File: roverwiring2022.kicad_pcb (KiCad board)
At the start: 2 copper layers, 78.7 x 116.8 mm, 20 parts, among them J1 Conn_01x19, J10 Conn_01x05, J11 Conn_01x05, J12 Conn_01x05, J13 Conn_01x05, J2 Conn_01x19, J3 Conn_01x09, J4 Conn_01x04, J5 Conn_01x04, J6 Conn_01x04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

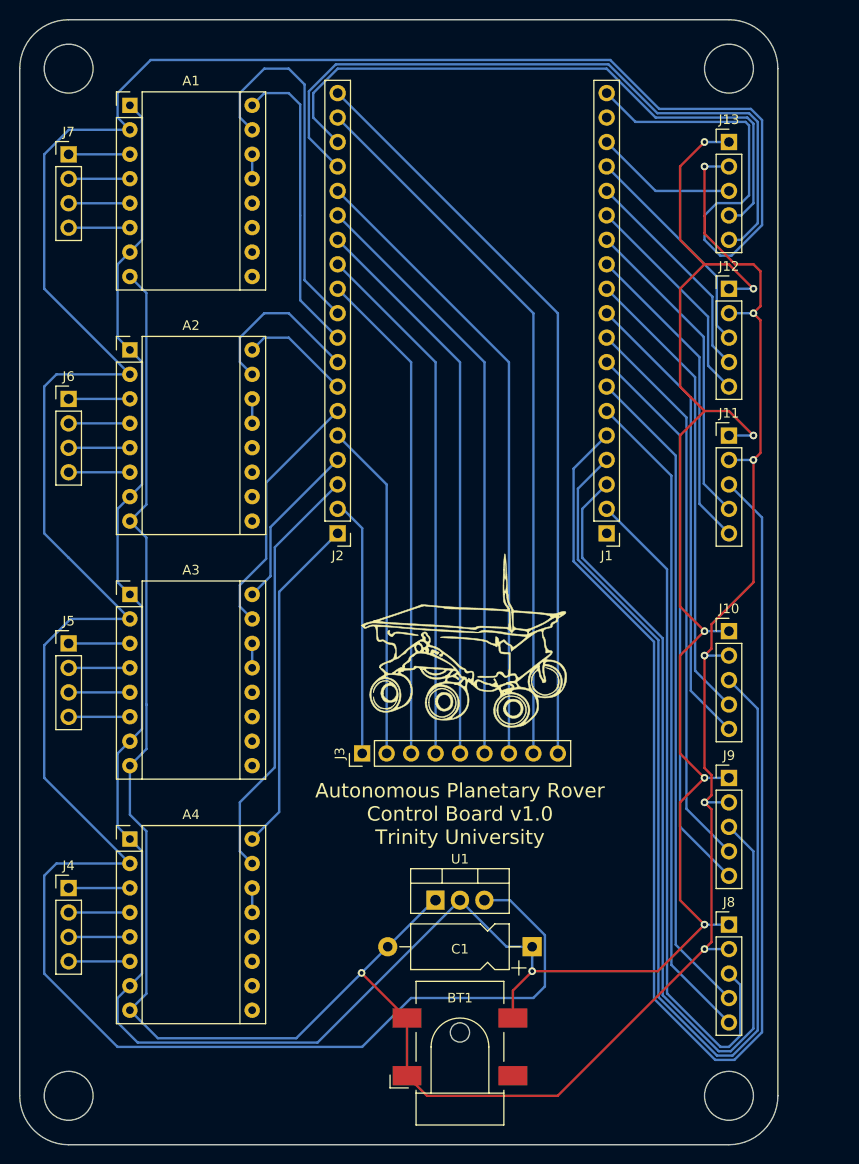
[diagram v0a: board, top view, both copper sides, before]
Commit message: updating traces to clear drc errors, widening power traces
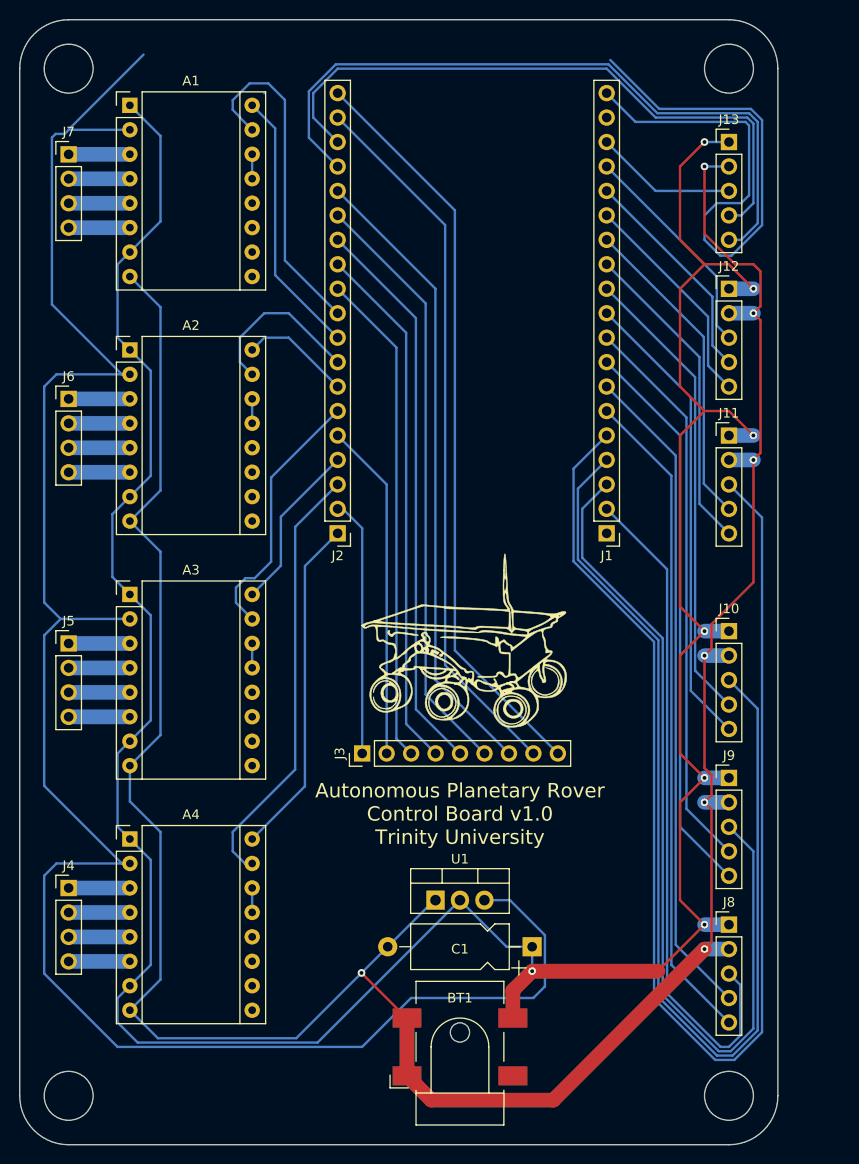
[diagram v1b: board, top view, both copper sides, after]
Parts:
- BT1: value 24V -> 12V
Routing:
- net /VDD: track 326.2 -> 278.8 mm
- net GND: track 302.6 -> 306.9 mm
- net Net-(A1-Pad16): track 31.8 -> 27.8 mm
- net /VCC: track 274.3 -> 278.3 mm
- net Net-(A1-Pad15): track 38.0 -> 35.2 mm
- net Net-(A4-Pad15): track 44.1 -> 45.2 mm
- net Net-(A3-Pad15): track 26.3 -> 27.2 mm

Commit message: resolved all outstanding drc conflicts and finished VCC and GND planes
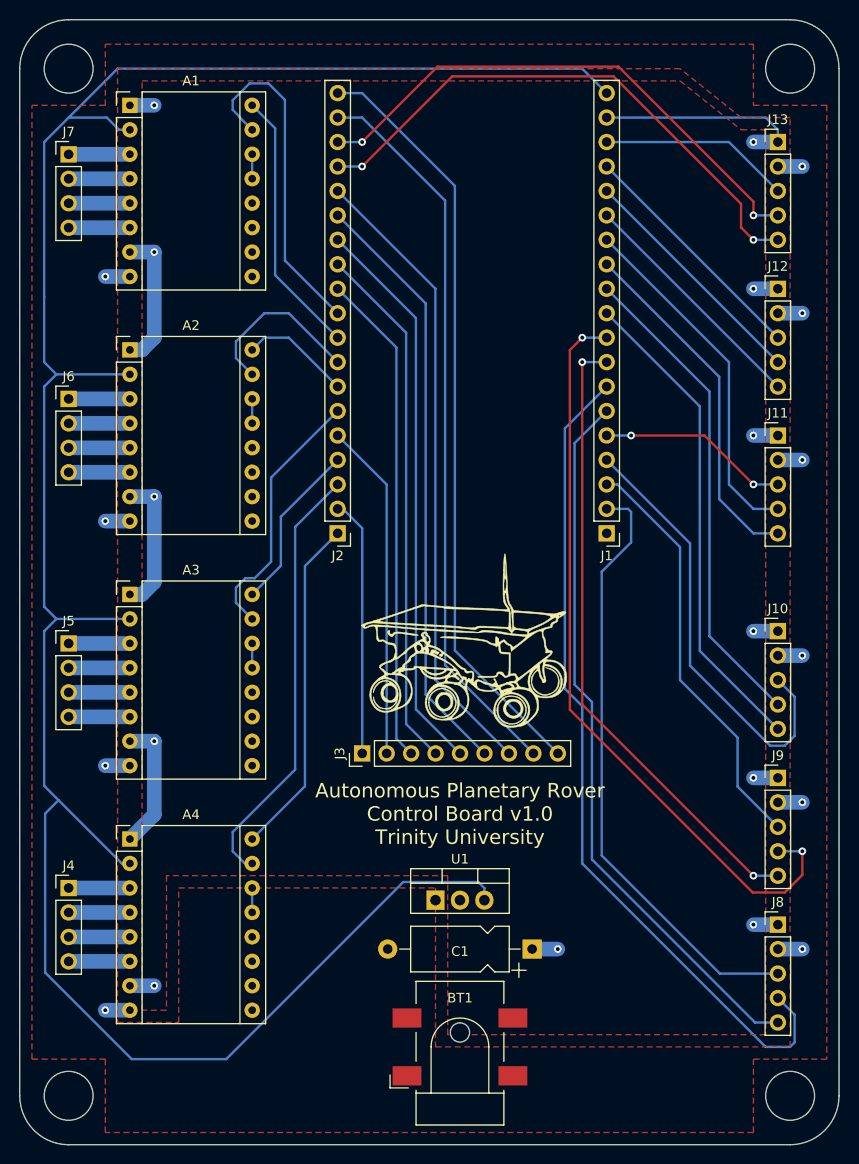
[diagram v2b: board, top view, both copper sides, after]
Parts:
- moved J10 5.08 mm to (261.6, 104.1)
- moved J11 5.08 mm to (261.6, 83.8)
- moved J12 5.08 mm to (261.6, 68.6)
- moved J13 5.08 mm to (261.6, 53.3)
- moved J8 5.08 mm to (261.6, 134.6)
- moved J9 5.08 mm to (261.6, 119.4)
- moved C1 0.24 mm to (236.1, 137.2)
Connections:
- J1 pad 18: unconnected-(J1-Pad18) -> GND
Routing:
- net /VCC: track 278.3 -> 25.4 mm, vias 7 -> 10
- net GND: track 306.9 -> 85.3 mm, vias 7 -> 12
- net Net-(J1-Pad5): track 136.7 -> 19.9 mm, vias 0 -> 2
- net Net-(J1-Pad4): track 112.0 -> 46.2 mm
- net Net-(J1-Pad3): track 92.4 -> 43.6 mm
- net /VDD: track 278.8 -> 242.9 mm
- net Net-(J1-Pad9): track 58.6 -> 79.5 mm, vias 0 -> 2
- net Net-(J1-Pad7): track 68.8 -> 87.5 mm
- net Net-(J13-Pad5): track 73.5 -> 58.1 mm, vias 0 -> 2
- net Net-(J13-Pad4): track 66.6 -> 56.2 mm, vias 0 -> 2
- net Net-(J1-Pad2): track 70.2 -> 63.0 mm
- net Net-(J1-Pad8): track 58.6 -> 65.8 mm, vias 0 -> 2
- net Net-(J1-Pad6): track 68.8 -> 75.0 mm
- net Net-(J1-Pad17): track 14.8 -> 19.9 mm
- net Net-(J1-Pad13): track 33.2 -> 36.8 mm
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- added copper zone on F.Cu, net /VCC
- added copper zone on F.Cu, net GND
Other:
- board size 78.7 x 116.8 mm -> 85.1 x 116.8 mm

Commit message: reshaped power planes, fixed gnd issue
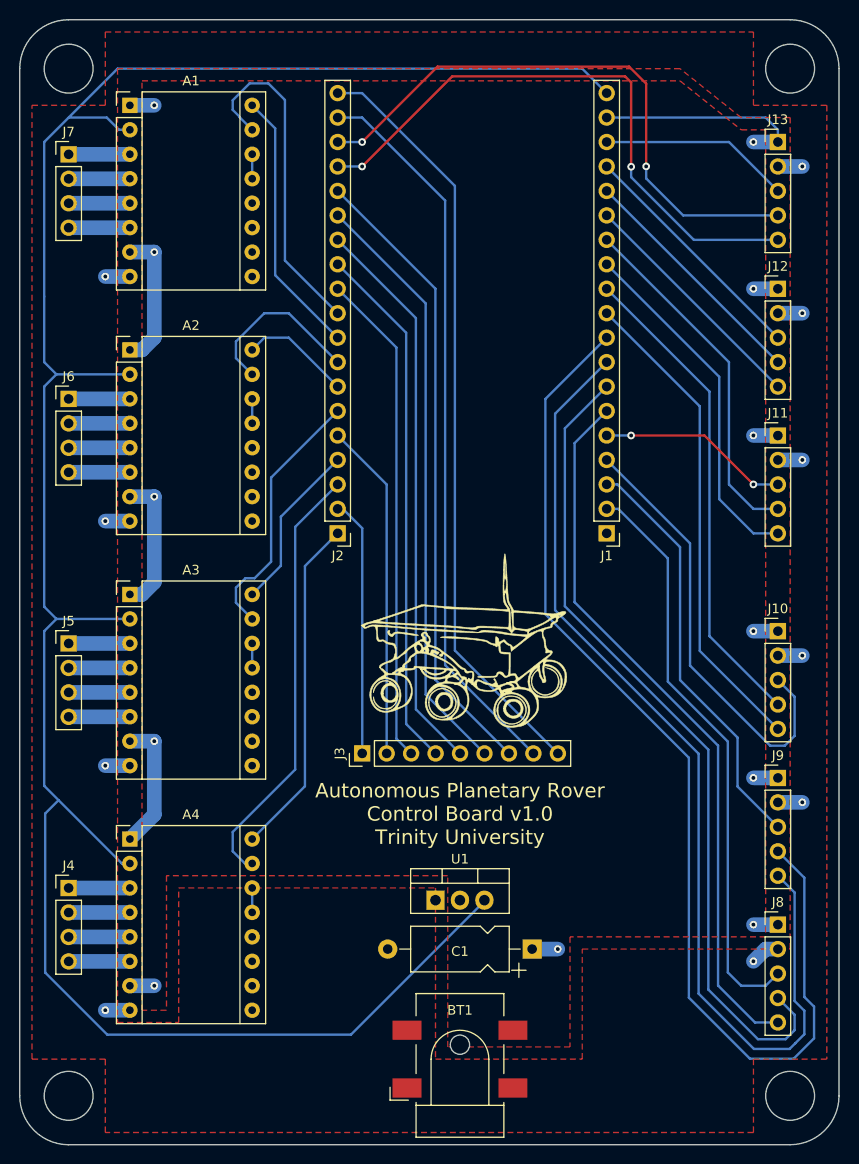
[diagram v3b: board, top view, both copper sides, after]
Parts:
- moved BT1 1.27 mm to (228.6, 148.6)
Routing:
- net Net-(J1-Pad8): track 65.8 -> 105.6 mm, vias 2 -> 0
- net Net-(J1-Pad9): track 79.5 -> 114.8 mm, vias 2 -> 0
- net Net-(J13-Pad4): track 56.2 -> 61.1 mm
- net /VDD: track 242.9 -> 238.6 mm
- net Net-(J13-Pad5): track 58.1 -> 62.4 mm
- net Net-(J1-Pad2): track 63.0 -> 60.4 mm
- net Net-(J1-Pad7): track 87.5 -> 86.1 mm
- net /VCC: track 25.4 -> 26.0 mm

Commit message: added backside ground plane
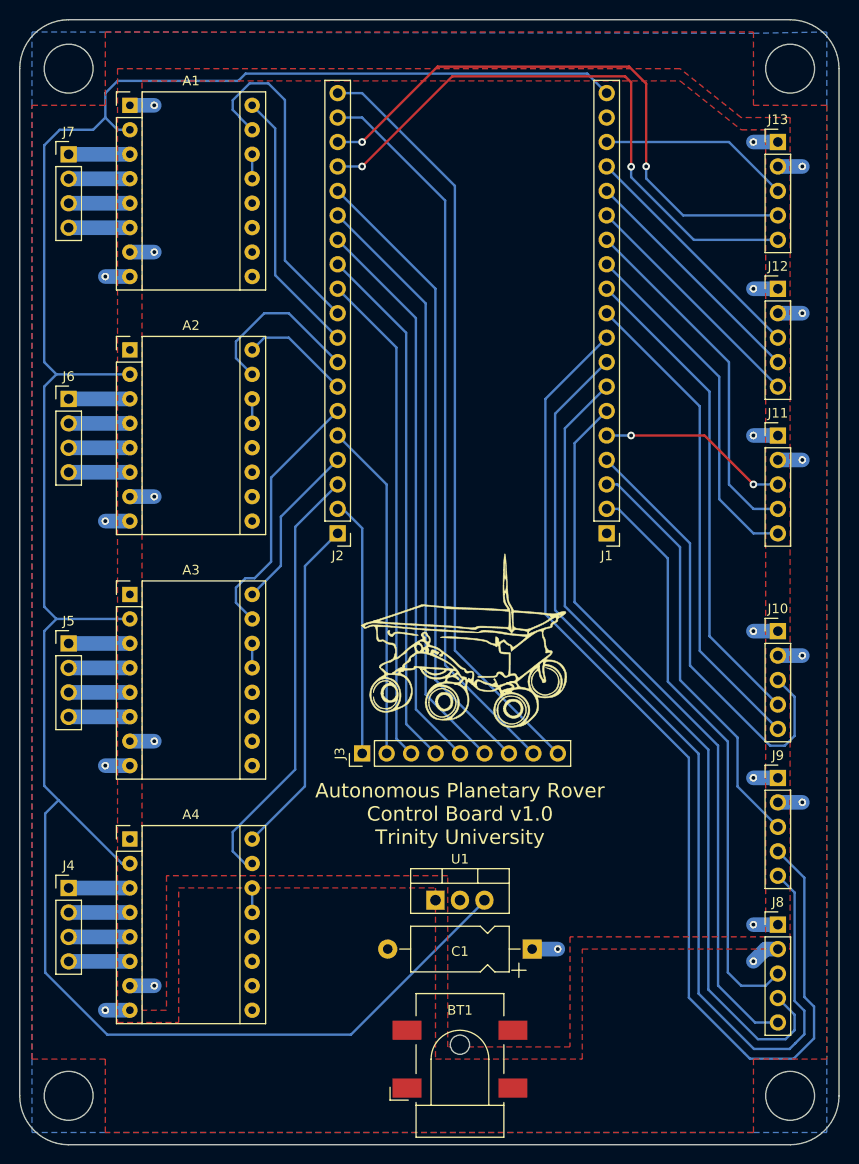
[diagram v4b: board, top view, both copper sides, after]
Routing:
- net GND: track 85.3 -> 30.7 mm
- net /VDD: track 238.6 -> 235.6 mm
- added copper zone on B.Cu, net GND
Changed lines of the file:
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@@
   )
   (segment (start 194.32 102.87) (end 186.69 102.87) (width 0.25) (layer "B.Cu") (net 1))
-  (segment (start 193.18863 52.07) (end 191.91863 50.8) (width 0.25) (layer "B.Cu") (net 1))
   (segment (start 185.521819 123.088181) (end 186.913 121.697) (width 0.25) (layer "B.Cu") (net 1))
+  (segment (start 241.81648 46.23648) (end 243.84 48.26) (width 0.25) (layer "B.Cu") (net 1))
   (segment (start 217.278267 146.05) (end 191.973638 146.05) (width 0.25) (layer "B.Cu") (net 1))
   (segment (start 194.32 77.47) (end 186.69 77.47) (width 0.25) (layer "B.Cu") (net 1))
+  (segment (start 187.036978 52.07) (end 190.5 52.07) (width 0.25) (layer "B.Cu") (net 1))
   (segment (start 186.69 102.87) (end 185.42 104.14) (width 0.25) (layer "B.Cu") (net 1))
   (segment (start 191.973638 146.05) (end 185.521819 139.598181) (width 0.25) (layer "B.Cu") (net 1))
+  (segment (start 185.42 53.686978) (end 187.036978 52.07) (width 0.25) (layer "B.Cu") (net 1))
+  (segment (start 191.77 48.26) (end 193.04 46.99) (width 0.25) (layer "B.Cu") (net 1))
   (segment (start 185.42 101.6) (end 186.69 102.87) (width 0.25) (layer "B.Cu") (net 1))
   (segment (start 185.42 120.204) (end 186.913 121.697) (width 0.25) (layer "B.Cu") (net 1))
   (segment (start 185.521819 139.598181) (end 185.521819 123.088181) (width 0.25) (layer "B.Cu") (net 1))
   (segment (start 185.42 78.74) (end 185.42 101.6) (width 0.25) (layer "B.Cu") (net 1))
+  (segment (start 205.579494 46.99) (end 206.333015 46.23648) (width 0.25) (layer "B.Cu") (net 1))
   (segment (start 186.69 77.47) (end 185.42 78.74) (width 0.25) (layer "B.Cu") (net 1))
   (segment (start 231.14 132.08) (end 231.14 132.188267) (width 0.25) (layer "B.Cu") (net 1))
+  (segment (start 194.32 52.07) (end 193.04 52.07) (width 0.25) (layer "B.Cu") (net 1))
+  (segment (start 186.69 77.47) (end 185.42 76.2) (width 0.25) (layer "B.Cu") (net 1))
   (segment (start 193.486 128.27) (end 194.32 128.27) (width 0.25) (layer "B.Cu") (net 1))
+  (segment (start 185.42 76.2) (end 185.42 53.686978) (width 0.25) (layer "B.Cu") (net 1))
   (segment (start 231.14 132.188267) (end 217.278267 146.05) (width 0.25) (layer "B.Cu") (net 1))
   (segment (start 186.913 121.697) (end 193.486 128.27) (width 0.25) (layer "B.Cu") (net 1))
-  (segment (start 191.91863 50.8) (end 187.96 50.8) (width 0.25) (layer "B.Cu") (net 1))
+  (segment (start 193.04 46.99) (end 205.579494 46.99) (width 0.25) (layer "B.Cu") (net 1))
   (segment (start 185.42 104.14) (end 185.42 120.204) (width 0.25) (layer "B.Cu") (net 1))
-  (segment (start 241.3 45.72) (end 243.84 48.26) (width 0.25) (layer "B.Cu") (net 1))
-  (segment (start 194.32 52.07) (end 193.18863 52.07) (width 0.25) (layer "B.Cu") (net 1))
-  (segment (start 185.42 69.404) (end 185.42 53.34) (width 0.25) (layer "B.Cu") (net 1))
-  (segment (start 185.42 69.404) (end 185.42 76.2) (width 0.25) (layer "B.Cu") (net 1))
-  (segment (start 185.42 76.2) (end 186.69 77.47) (width 0.25) (layer "B.Cu") (net 1))
-  (segment (start 193.04 45.72) (end 241.3 45.72) (width 0.25) (layer "B.Cu") (net 1))
-  (segment (start 185.42 53.34) (end 193.04 45.72) (width 0.25) (layer "B.Cu") (net 1))
+  (segment (start 190.5 52.07) (end 191.77 50.8) (width 0.25) (layer "B.Cu") (net 1))
+  (segment (start 193.04 52.07) (end 191.77 50.8) (width 0.25) (layer "B.Cu") (net 1))
+  (segment (start 206.333015 46.23648) (end 241.81648 46.23648) (width 0.25) (layer "B.Cu") (net 1))
+  (segment (start 191.77 50.8) (end 191.77 48.26) (width 0.25) (layer "B.Cu") (net 1))
   (segment (start 194.31 54.62) (end 194.32 54.61) (width 0.25) (layer "B.Cu") (net 2))
   (segment (start 187.96 54.62) (end 194.31 54.62) (width 1.524) (layer "B.Cu") (net 2))
@@
   (segment (start 263.356511 131.281511) (end 261.62 129.545) (width 0.25) (layer "B.Cu") (net 54))
   (segment (start 264.368031 146.002475) (end 264.368031 143.562525) (width 0.25) (layer "B.Cu") (net 54))
-  (segment (start 263.25646 148.544551) (end 258.71354 148.544551) (width 0.25) (layer "B.Cu") (net 55))
-  (segment (start 252.37388 142.204891) (end 252.37388 117.28641) (width 0.25) (layer "B.Cu") (net 55))
-  (segment (start 261.62 127.005) (end 264.368031 129.753031) (width 0.25) (layer "B.Cu") (net 55))
-  (segment (start 265.37955 146.421461) (end 263.25646 148.544551) (width 0.25) (layer "B.Cu") (net 55))
-  (segment (start 258.71354 148.544551) (end 252.37388 142.204891) (width 0.25) (layer "B.Cu") (net 55))
   (segment (start 237.471951 102.38448) (end 237.471951 80.028049) (width 0.25) (layer "B.Cu") (net 55))
   (segment (start 264.368031 142.132021) (end 265.379551 143.14354) (width 0.25) (layer "B.Cu") (net 55))
+  (segment (start 252.37388 142.20489) (end 252.37388 117.28641) (width 0.25) (layer "B.Cu") (net 55))
+  (segment (start 252.37388 117.28641) (end 237.471951 102.38448) (width 0.25) (layer "B.Cu") (net 55))
+  (segment (start 258.71354 148.544551) (end 258.121006 147.952016) (width 0.25) (layer "B.Cu") (net 55))
+  (segment (start 261.62 127.005) (end 264.368031 129.753031) (width 0.25) (layer "B.Cu") (net 55))
+  (segment (start 264.368031 129.753031) (end 264.368031 142.132021) (width 0.25) (layer "B.Cu") (net 55))
+  (segment (start 265.37955 146.421461) (end 263.25646 148.544551) (width 0.25) (layer "B.Cu") (net 55))
+  (segment (start 263.25646 148.544551) (end 258.71354 148.544551) (width 0.25) (layer "B.Cu") (net 55))
   (segment (start 237.471951 80.028049) (end 243.84 73.66) (width 0.25) (layer "B.Cu") (net 55))
-  (segment (start 252.37388 117.28641) (end 237.471951 102.38448) (width 0.25) (layer "B.Cu") (net 55))
   (segment (start 265.379551 143.14354) (end 265.37955 146.421461) (width 0.25) (layer "B.Cu") (net 55))
-  (segment (start 264.368031 129.753031) (end 264.368031 142.132021) (width 0.25) (layer "B.Cu") (net 55))
+  (segment (start 258.121006 147.952016) (end 252.37388 142.20489) (width 0.25) (layer "B.Cu") (net 55))
   (segment (start 253.50544 106.18544) (end 261.62 114.3) (width 0.25) (layer "B.Cu") (net 56))
   (segment (start 253.50544 80.78544) (end 253.50544 106.18544) (width 0.25) (layer "B.Cu") (net 56))
@@
   (segment (start 194.304996 140.97) (end 196.855004 140.97) (width 1.524) (layer "B.Cu") (net 75))
   (segment (start 194.304996 64.77) (end 196.855004 64.77) (width 1.524) (layer "B.Cu") (net 75))
-  (segment (start 196.855004 64.77) (end 196.855004 73.654996) (width 1.524) (layer "B.Cu") (net 75))
   (segment (start 194.304996 115.57) (end 196.855004 115.57) (width 1.524) (layer "B.Cu") (net 75))
-  (segment (start 196.855004 99.054996) (end 195.58 100.33) (width 1.524) (layer "B.Cu") (net 75))
-  (segment (start 261.62 52.07) (end 261.62 53.34) (width 0.25) (layer "B.Cu") (net 75))
   (segment (start 261.62 53.34) (end 259.08 53.34) (width 1.524) (layer "B.Cu") (net 75))
-  (segment (start 195.58 100.33) (end 194.32 100.33) (width 1.524) (layer "B.Cu") (net 75))
   (segment (start 238.759975 137.16) (end 236.10001 137.16) (width 1.524) (layer "B.Cu") (net 75))
-  (segment (start 195.58 74.93) (end 194.32 74.93) (width 1.524) (layer "B.Cu") (net 75))
   (segment (start 261.62 104.14) (end 259.08 104.14) (width 1.524) (layer "B.Cu") (net 75))
   (segment (start 261.62 119.38) (end 259.08 119.38) (width 1.524) (layer "B.Cu") (net 75))
   (segment (start 259.085 134.625) (end 261.62 134.625) (width 1.524) (layer "B.Cu") (net 75))
   (segment (start 238.759994 137.16001) (end 238.759984 137.16) (width 0.25) (layer "B.Cu") (net 75))
-  (segment (start 196.855004 115.57) (end 196.855004 123.194996) (width 1.524) (layer "B.Cu") (net 75))
-  (segment (start 260.35 50.8) (end 261.62 52.07) (width 0.25) (layer "B.Cu") (net 75))
-  (segment (start 196.855004 123.194996) (end 194.32 125.73) (width 1.524) (layer "B.Cu") (net 75))
   (segment (start 261.62 83.82) (end 259.08 83.82) (width 1.524) (layer "B.Cu") (net 75))
   (segment (start 259.08 134.62) (end 259.085 134.625) (width 0.25) (layer "B.Cu") (net 75))
   (segment (start 261.62 68.58) (end 259.08 68.58) (width 1.524) (layer "B.Cu") (net 75))
-  (segment (start 196.855004 90.17) (end 196.855004 99.054996) (width 1.524) (layer "B.Cu") (net 75))
   (segment (start 194.304996 90.17) (end 196.855004 90.17) (width 1.524) (layer "B.Cu") (net 75))
-  (segment (start 243.84 50.8) (end 260.35 50.8) (width 0.25) (layer "B.Cu") (net 75))
   (segment (start 194.299992 49.53) (end 196.85 49.53) (width 1.524) (layer "B.Cu") (net 75))
-  (segment (start 196.855004 73.654996) (end 195.58 74.93) (width 1.524) (layer "B.Cu") (net 75))
   (zone (net 75) (net_name "GND") (layer "F.Cu") (name "GND") (hatch edge 0.508)
     (connect_pads (clearance 0.762))
@@
       )
     )
+  )
+  (zone (net 75) (net_name "GND") (layer "B.Cu") (name "GND") (hatch edge 0.508)
+    (connect_pads (clearance 0.762))
+    (min_thickness 0.254) (filled_areas_thickness no)
+    (fill yes (thermal_gap 0.508) (thermal_bridge_width 0.508) (smoothing fillet) (radius 1.524))
+    (polygon
+      (pts
+        (xy 266.7 49.53)
+        (xy 266.7 148.59)
+        (xy 266.7 156.21)
+        (xy 259.08 156.21)
+        (xy 191.77 156.21)
+        (xy 184.15 156.21)
+        (xy 184.15 148.59)
+        (xy 184.15 49.53)
+        (xy 184.15 41.91)
+        (xy 191.769975 41.923905)
+        (xy 259.08 42.046737)
+        (xy 266.7 41.91)
+      )
+    )
